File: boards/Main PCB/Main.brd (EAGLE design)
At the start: 101.6 x 76.2 mm, 114 parts, among them CN1 MINIB, CN2 MINIB, IC1 FT232RL, IC2 FT232RL, IC4 OKR-T_3-W12-C, J1 3_PIN_JST-XH, J2 2_PIN_JST-XH, J3 5_PIN_JST-XH, Q4 BSS138, Q5 BSS138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

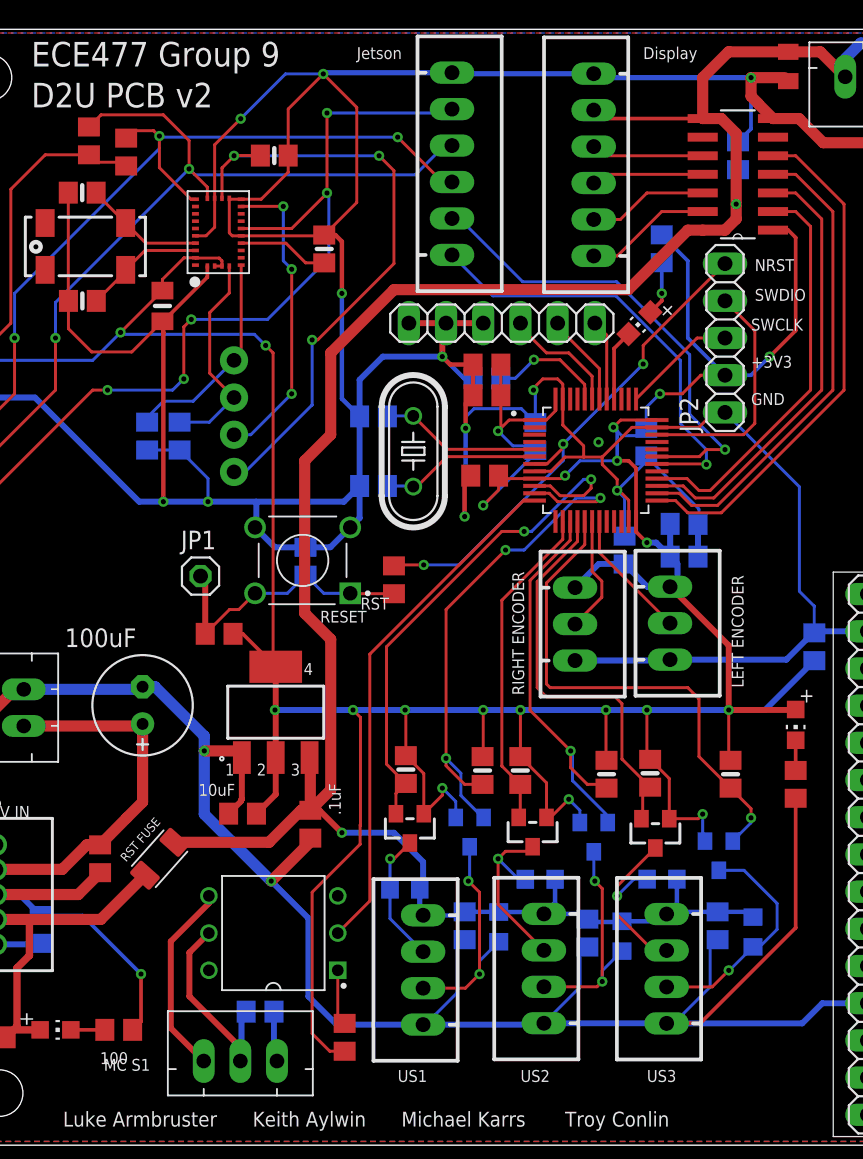
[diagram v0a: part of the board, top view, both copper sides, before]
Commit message: Fixing logic converter circuit
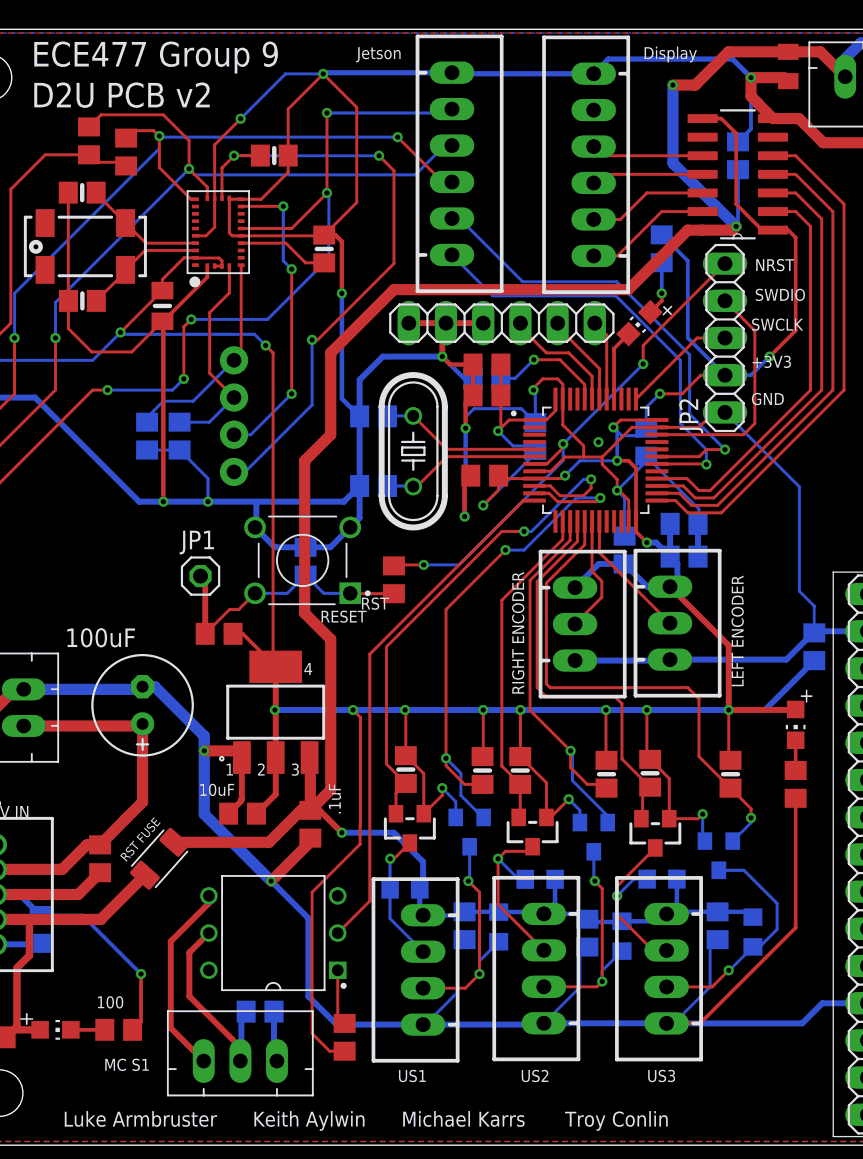
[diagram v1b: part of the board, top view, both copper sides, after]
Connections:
- net +3V3: now also U4.8
- net +5V: no longer U4.8
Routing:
- net +3V3: track 309.2 -> 320.0 mm
- net +5V: track 172.0 -> 168.9 mm, vias 2 -> 3
- net GND: track 763.6 -> 764.5 mm
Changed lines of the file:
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@@
 <attribute name="MP" value="TXS0104EDR" x="51.816" y="70.104" size="1.778" layer="27" rot="R180" display="off"/>
 <attribute name="PACKAGE" value="SOIC-14 Texas Instruments" x="51.816" y="70.104" size="1.778" layer="27" rot="R180" display="off"/>
-<attribute name="VALUE" x="49.55815" y="71.26255" size="0.6096" layer="27" ratio="10" rot="SR0"/>
+<attribute name="VALUE" x="49.55815" y="71.00855" size="0.6096" layer="27" ratio="10" rot="SR0"/>
 </element>
 <element name="JP4" library="microbuilder" package="1X04_ROUND_76" value="" x="19.812" y="49.784" smashed="yes" rot="R90">
@@
 <element name="R32" library="rcl" library_urn="urn:adsk.eagle:library:334" package="R0805" package3d_urn="urn:adsk.eagle:package:23553/2" value="100" x="11.938" y="7.874" smashed="yes" rot="R180">
 <attribute name="SPICEPREFIX" value="R" x="11.938" y="7.874" size="1.778" layer="27" rot="R180" display="off"/>
-<attribute name="VALUE" x="12.573" y="6.35" size="0.8128" layer="25" rot="R180"/>
+<attribute name="VALUE" x="12.319" y="10.16" size="0.8128" layer="25" rot="R180"/>
 </element>
 <element name="R33" library="RESET_FUSE" package="RESC3216X125N" value="0ZCJ0050FF2G" x="14.732" y="19.558" smashed="yes" rot="R48.3">
@@
 <attribute name="MOUSER_PART_NUMBER" value="580-OKR-T/3-W12-C" x="3.556" y="13.716" size="1.778" layer="27" rot="R90" display="off"/>
 <attribute name="MOUSER_PRICE-STOCK" value="https://www.mouser.com/Search/Refine.aspx?Keyword=580-OKR-T%2F3-W12-C" x="3.556" y="13.716" size="1.778" layer="27" rot="R90" display="off"/>
-<attribute name="VALUE" x="8.284" y="16.578" size="1.27" layer="27" rot="R90" align="center"/>
 </element>
 <element name="R36" library="rcl" library_urn="urn:adsk.eagle:library:334" package="R0805" package3d_urn="urn:adsk.eagle:package:23553/2" value="270" x="6.604" y="14.732" smashed="yes" rot="MR270">
@@
 </element>
 <element name="R37" library="resistor" library_urn="urn:adsk.eagle:library:348" package="R0805" package3d_urn="urn:adsk.eagle:package:26059/1" value="100" x="30.734" y="38.608" smashed="yes" rot="R270">
-<attribute name="VALUE" x="30.734" y="38.989" size="1.27" layer="27" rot="R270"/>
+<attribute name="VALUE" x="32.004" y="38.989" size="0.6096" layer="27" rot="R270"/>
 </element>
 <element name="JP2" library="pinhead" library_urn="urn:adsk.eagle:library:325" package="1X05" package3d_urn="urn:adsk.eagle:package:22469/2" value="" x="53.34" y="55.118" smashed="yes" rot="R90">
@@
 <wire x1="25.908" y1="73.152" x2="25.993" y2="73.237" width="0.3556" layer="16"/>
 <via x="55.118" y="72.898" extent="1-16" drill="0.35"/>
-<wire x1="55.118" y1="72.898" x2="44.645" y2="72.898" width="0.3556" layer="16"/>
-<wire x1="44.645" y1="72.898" x2="44.374" y2="73.169" width="0.3048" layer="16"/>
+<wire x1="55.118" y1="72.898" x2="53.848" y2="74.168" width="0.3556" layer="16"/>
+<wire x1="53.848" y1="74.168" x2="45.373" y2="74.168" width="0.3556" layer="16"/>
+<wire x1="44.374" y1="73.169" x2="45.373" y2="74.168" width="0.3556" layer="16"/>
 <wire x1="44.374" y1="73.169" x2="34.766" y2="73.169" width="0.3556" layer="16"/>
 <wire x1="34.766" y1="73.169" x2="34.698" y2="73.237" width="0.3048" layer="16"/>
@@
 <wire x1="53.594" y1="34.1252" x2="49.585" y2="38.1342" width="0.4064" layer="1"/>
 <wire x1="49.585" y1="38.1342" x2="48.0378" y2="38.1342" width="0.4064" layer="16"/>
+<contactref element="U4" pad="8"/>
+<wire x1="56.6166" y1="62.484" x2="55.88" y2="62.484" width="0.254" layer="1"/>
+<wire x1="55.88" y1="62.484" x2="54.102" y2="64.262" width="0.254" layer="1"/>
+<wire x1="54.102" y1="64.262" x2="54.102" y2="69.088" width="0.254" layer="1"/>
+<wire x1="54.102" y1="69.088" x2="53.086" y2="70.104" width="0.254" layer="1"/>
+<wire x1="53.086" y1="70.104" x2="51.816" y2="70.104" width="0.254" layer="1"/>
 </signal>
 <signal name="N$6">
@@
 <contactref element="X1" pad="5"/>
 <contactref element="U4" pad="14"/>
-<contactref element="U4" pad="8"/>
-<wire x1="51.816" y1="70.104" x2="53.086" y2="70.104" width="0.762" layer="1"/>
-<wire x1="53.086" y1="70.104" x2="54.102" y2="69.088" width="0.762" layer="1"/>
-<wire x1="54.102" y1="69.088" x2="54.102" y2="64.262" width="0.762" layer="1"/>
-<wire x1="54.102" y1="64.262" x2="54.102" y2="63.246" width="0.762" layer="1"/>
-<wire x1="54.102" y1="63.246" x2="53.34" y2="62.484" width="0.762" layer="1"/>
-<wire x1="53.34" y1="62.484" x2="51.816" y2="62.484" width="0.762" layer="1"/>
-<wire x1="51.816" y1="70.104" x2="44.9498" y2="70.104" width="0.254" layer="1"/>
+<wire x1="54.102" y1="62.738" x2="53.848" y2="62.484" width="0.762" layer="1"/>
+<wire x1="53.848" y1="62.484" x2="51.816" y2="62.484" width="0.762" layer="1"/>
 <wire x1="44.9498" y1="70.104" x2="44.374" y2="70.6798" width="0.254" layer="1"/>
 <wire x1="26.416" y1="24.262" x2="26.416" y2="34.544" width="0.762" layer="1"/>
@@
 <wire x1="54.884" y1="15.936" x2="55.246" y2="15.574" width="0.3048" layer="16"/>
 <contactref element="C27" pad="1"/>
-<via x="54.102" y="64.262" extent="1-16" drill="0.35"/>
-<wire x1="54.102" y1="64.262" x2="54.229" y2="64.389" width="0.254" layer="16"/>
-<wire x1="54.229" y1="64.389" x2="54.229" y2="66.614" width="0.254" layer="16"/>
+<via x="54.102" y="62.738" extent="1-16" drill="0.35"/>
+<wire x1="54.102" y1="62.738" x2="54.229" y2="62.738" width="0.254" layer="16"/>
+<wire x1="54.229" y1="62.738" x2="54.229" y2="66.614" width="0.254" layer="16"/>
 <wire x1="35.56" y1="15.936" x2="37.874" y2="15.936" width="0.3048" layer="16"/>
 <wire x1="37.874" y1="15.936" x2="37.888" y2="15.922" width="0.3556" layer="16"/>
@@
 <wire x1="61.548" y1="74.1972" x2="61.548" y2="72.958" width="0.508" layer="16"/>
 <contactref element="D1" pad="C"/>
-<wire x1="51.816" y1="72.898" x2="53.594" y2="74.676" width="0.762" layer="1"/>
-<wire x1="51.816" y1="72.898" x2="51.816" y2="70.104" width="0.762" layer="1"/>
 <wire x1="71.548" y1="72.958" x2="71.548" y2="74.502" width="0.762" layer="16"/>
 <wire x1="71.548" y1="74.502" x2="70.7898" y2="75.2602" width="0.762" layer="16"/>
@@
 <wire x1="24.638" y1="46.736" x2="26.416" y2="48.514" width="0.762" layer="1"/>
 <wire x1="24.638" y1="36.322" x2="24.638" y2="46.736" width="0.762" layer="1"/>
+<wire x1="54.102" y1="62.738" x2="49.784" y2="67.056" width="0.762" layer="16"/>
+<wire x1="49.784" y1="67.056" x2="49.784" y2="72.39" width="0.762" layer="16"/>
+<via x="49.784" y="72.39" extent="1-16" drill="0.35"/>
+<wire x1="49.784" y1="72.39" x2="51.308" y2="72.39" width="0.762" layer="1"/>
+<wire x1="51.308" y1="72.39" x2="53.594" y2="74.676" width="0.762" layer="1"/>
+<wire x1="49.784" y1="67.056" x2="44.9498" y2="70.104" width="0" layer="19" extent="1-16"/>
 </signal>
 <signal name="N$5">

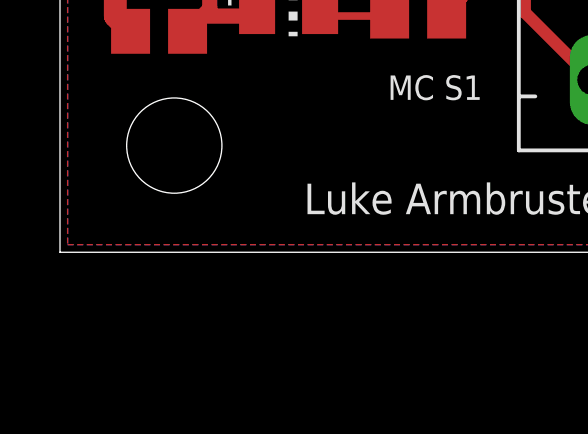
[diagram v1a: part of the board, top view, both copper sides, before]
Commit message: Adding decoupling cap at 3V into logic converter
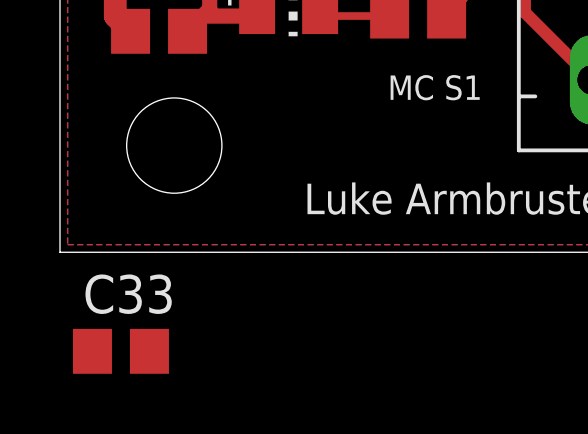
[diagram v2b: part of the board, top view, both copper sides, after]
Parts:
- added C33: .1uF, rcl:C0805
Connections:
- net +3V3: now also C33.1
- net GND: now also C33.2
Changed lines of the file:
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@@
 <attribute name="VALUE" x="16.256" y="35.687" size="1.27" layer="27"/>
+</element>
+<element name="C33" library="rcl" library_urn="urn:adsk.eagle:library:334" package="C0805" package3d_urn="urn:adsk.eagle:package:23617/2" value=".1uF" x="2.032" y="-3.302" smashed="yes">
+<attribute name="NAME" x="0.762" y="-2.032" size="1.27" layer="25"/>
+<attribute name="SPICEPREFIX" value="C" x="2.032" y="-3.302" size="1.778" layer="27" display="off"/>
+<attribute name="VALUE" x="0.762" y="-5.842" size="1.27" layer="27"/>
 </element>
 </elements>
@@
 <wire x1="5.454" y1="31.126" x2="13.388" y2="31.126" width="0.762" layer="16"/>
 <wire x1="13.388" y1="31.126" x2="13.568" y2="31.306" width="0.762" layer="16"/>
+<contactref element="C33" pad="2"/>
+<wire x1="2.982" y1="-3.302" x2="2.352" y2="7.366" width="0" layer="19" extent="1-1"/>
 </signal>
 <signal name="D+_GPS">
@@
 <wire x1="54.102" y1="69.088" x2="53.086" y2="70.104" width="0.254" layer="1"/>
 <wire x1="53.086" y1="70.104" x2="51.816" y2="70.104" width="0.254" layer="1"/>
+<contactref element="C33" pad="1"/>
+<wire x1="1.082" y1="-3.302" x2="25.146" y2="7.62" width="0" layer="19" extent="1-1"/>
 </signal>
 <signal name="N$6">

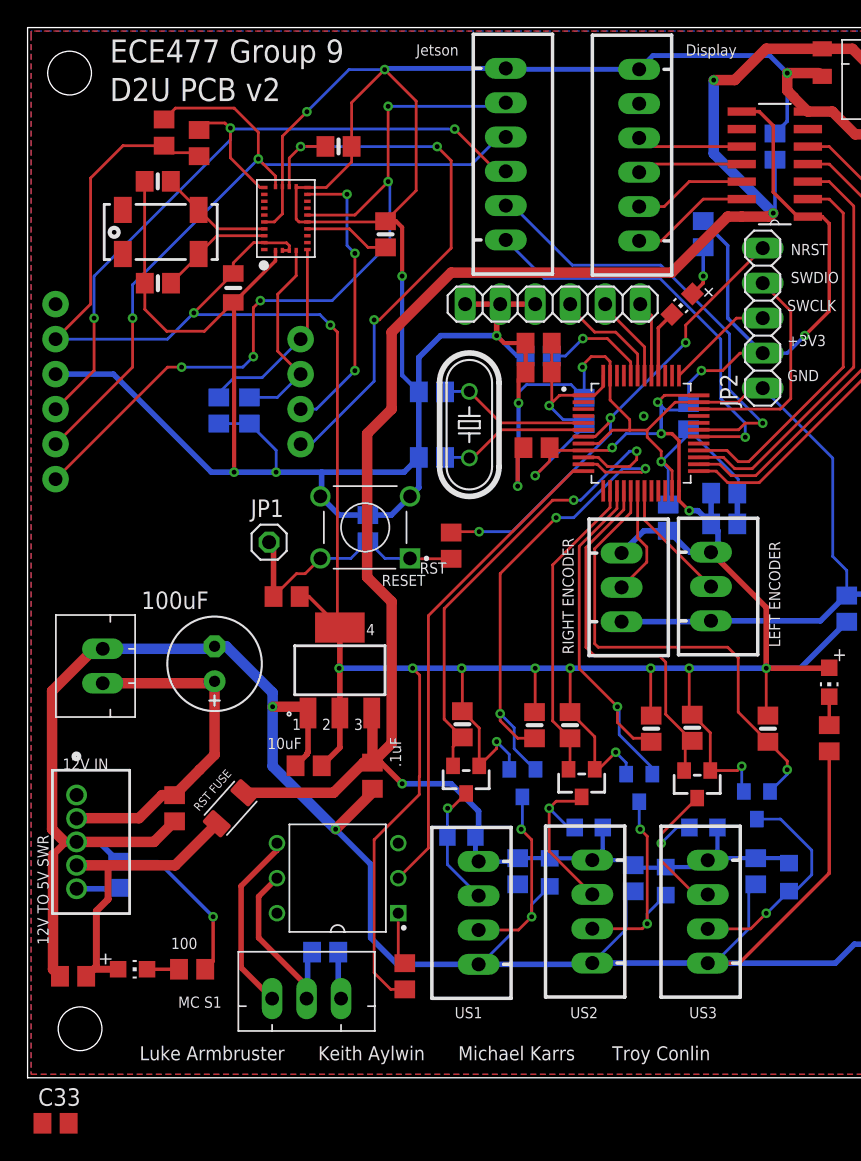
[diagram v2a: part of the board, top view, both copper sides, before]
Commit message: Adding decoupling cap at 3V into logic converter
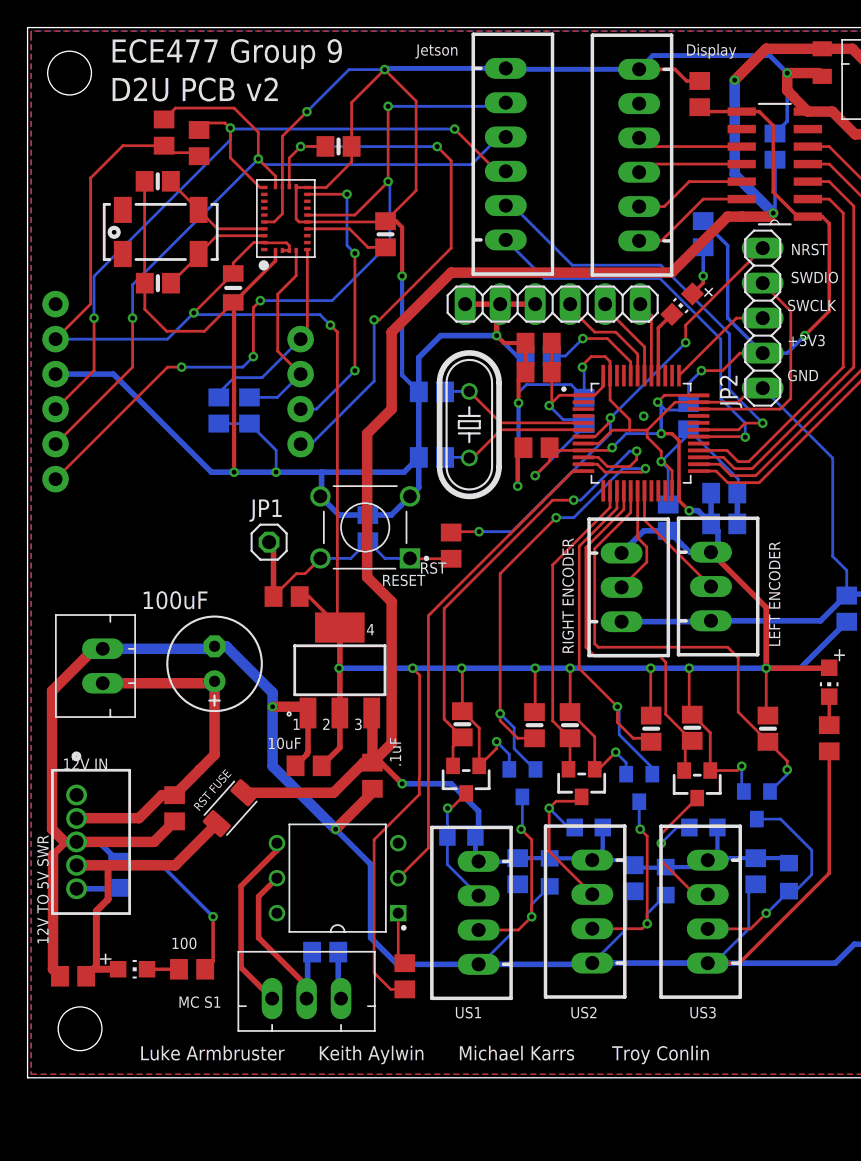
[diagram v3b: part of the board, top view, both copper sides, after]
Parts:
- moved C33 88.1 mm to (48.8, 71.4), turned to 90 degrees
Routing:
- net GND: track 764.5 -> 769.2 mm
- net +3V3: track 320.0 -> 323.2 mm
- net +5V: track 168.9 -> 166.7 mm
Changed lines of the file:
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@@
 <attribute name="VALUE" x="16.256" y="35.687" size="1.27" layer="27"/>
 </element>
-<element name="C33" library="rcl" library_urn="urn:adsk.eagle:library:334" package="C0805" package3d_urn="urn:adsk.eagle:package:23617/2" value=".1uF" x="2.032" y="-3.302" smashed="yes">
-<attribute name="NAME" x="0.762" y="-2.032" size="1.27" layer="25"/>
-<attribute name="SPICEPREFIX" value="C" x="2.032" y="-3.302" size="1.778" layer="27" display="off"/>
-<attribute name="VALUE" x="0.762" y="-5.842" size="1.27" layer="27"/>
+<element name="C33" library="rcl" library_urn="urn:adsk.eagle:library:334" package="C0805" package3d_urn="urn:adsk.eagle:package:23617/2" value=".1uF" x="48.768" y="71.374" smashed="yes" rot="R90">
+<attribute name="SPICEPREFIX" value="C" x="48.768" y="71.374" size="1.778" layer="27" rot="R90" display="off"/>
+<attribute name="VALUE" x="49.53" y="69.088" size="0.6096" layer="27" rot="R180"/>
 </element>
 </elements>
@@
 <wire x1="13.388" y1="31.126" x2="13.568" y2="31.306" width="0.762" layer="16"/>
 <contactref element="C33" pad="2"/>
-<wire x1="2.982" y1="-3.302" x2="2.352" y2="7.366" width="0" layer="19" extent="1-1"/>
+<wire x1="48.768" y1="72.324" x2="47.818" y2="72.324" width="0.254" layer="1"/>
+<wire x1="46.973" y1="73.169" x2="44.374" y2="73.169" width="0.254" layer="1"/>
+<wire x1="47.818" y1="72.324" x2="46.973" y2="73.169" width="0.254" layer="1"/>
 </signal>
 <signal name="D+_GPS">
@@
 <wire x1="53.086" y1="70.104" x2="51.816" y2="70.104" width="0.254" layer="1"/>
 <contactref element="C33" pad="1"/>
-<wire x1="1.082" y1="-3.302" x2="25.146" y2="7.62" width="0" layer="19" extent="1-1"/>
+<wire x1="51.816" y1="70.104" x2="49.088" y2="70.104" width="0.254" layer="1"/>
+<wire x1="49.088" y1="70.104" x2="48.768" y2="70.424" width="0.254" layer="1"/>
 </signal>
 <signal name="N$6">
@@
 <wire x1="24.638" y1="46.736" x2="26.416" y2="48.514" width="0.762" layer="1"/>
 <wire x1="24.638" y1="36.322" x2="24.638" y2="46.736" width="0.762" layer="1"/>
-<wire x1="54.102" y1="62.738" x2="49.784" y2="67.056" width="0.762" layer="16"/>
-<wire x1="49.784" y1="67.056" x2="49.784" y2="72.39" width="0.762" layer="16"/>
-<via x="49.784" y="72.39" extent="1-16" drill="0.35"/>
-<wire x1="49.784" y1="72.39" x2="51.308" y2="72.39" width="0.762" layer="1"/>
+<wire x1="54.102" y1="62.738" x2="51.308" y2="65.532" width="0.762" layer="16"/>
+<wire x1="51.308" y1="65.532" x2="51.308" y2="72.39" width="0.762" layer="16"/>
+<via x="51.308" y="72.39" extent="1-16" drill="0.35"/>
 <wire x1="51.308" y1="72.39" x2="53.594" y2="74.676" width="0.762" layer="1"/>
-<wire x1="49.784" y1="67.056" x2="44.9498" y2="70.104" width="0" layer="19" extent="1-16"/>
+<wire x1="51.308" y1="65.532" x2="44.9498" y2="70.104" width="0" layer="19" extent="1-16"/>
 </signal>
 <signal name="N$5">
